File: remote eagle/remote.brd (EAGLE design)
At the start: 38.6 x 38.6 mm, 13 parts, among them J1 ISP Touch, Y1 8MHz

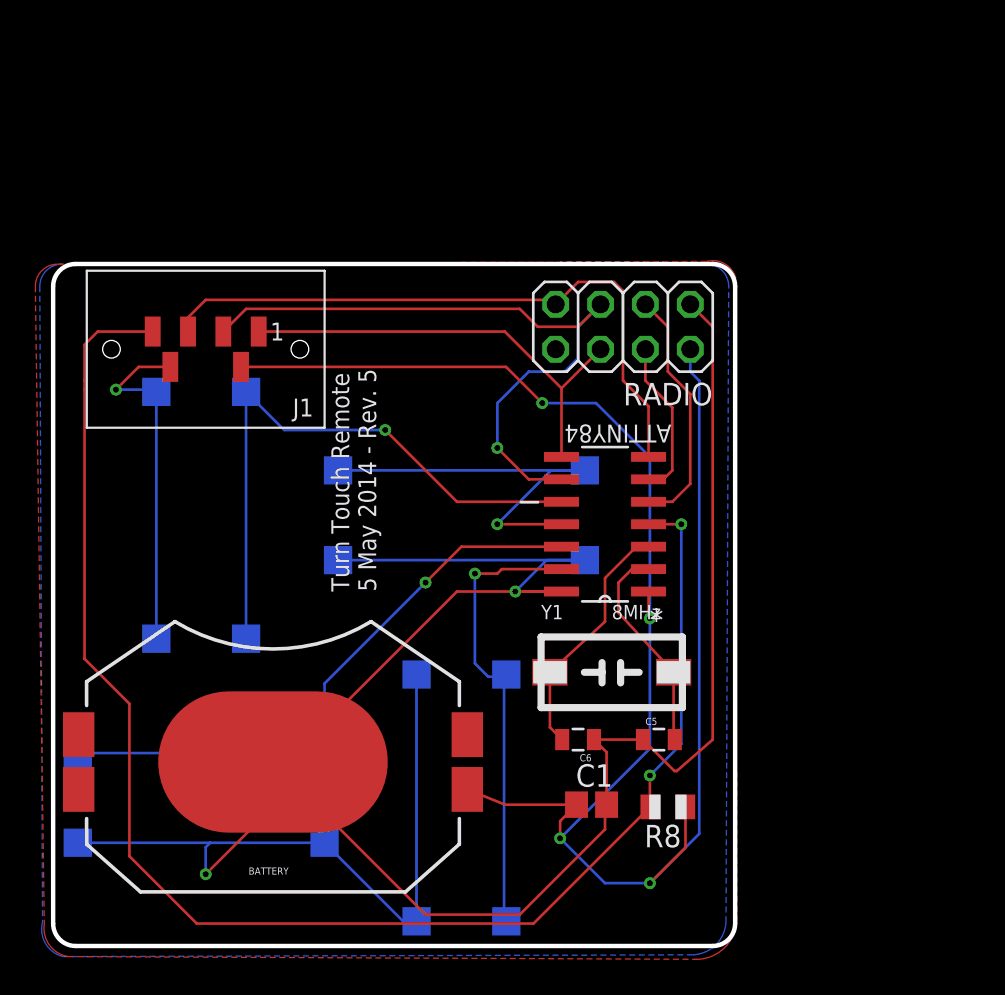
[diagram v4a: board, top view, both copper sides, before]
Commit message: Moving from nrf24L01+ module to onboard chip. Moving both MCU and radio IC to QFN package.
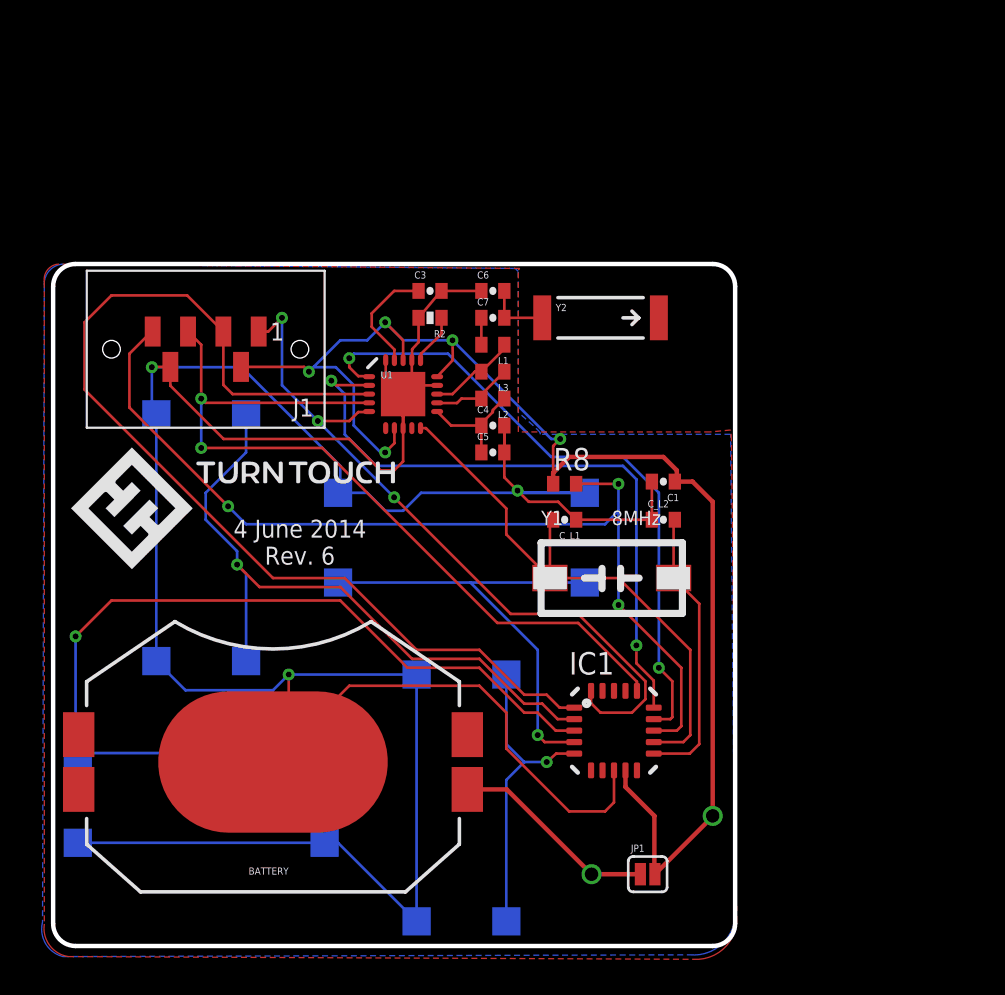
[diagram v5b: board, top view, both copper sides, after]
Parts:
- removed ATTINY84: (no value), Atmel_By_element14_Batch_1:SOIC127P600X175-14N
- removed RADIO: NRF24L01, pinhead:2X04
- added C3: 33nF, SparkFun:0402-CAP
- added C4: 2.2nF, SparkFun:0402-CAP
- added C7: 1.5pF, SparkFun:0402-CAP
- added C_L1, C_L2: 8pF, SparkFun-Passives:0402-CAP
- added IC1: TINY24/44/84-MU, avr-7:QFN/MLF20
- added JP1: (no value), SparkFun-Passives:SJ_2S
- added L1: 3.9nH, SparkFun:C0402
- added L2: 2.7nH, SparkFun:C0402
- added L3: 8.2nH, SparkFun:C0402
- added LOGO: (no value), remote:LOGO
- added R2: 22K, SparkFun:0402-RES
- added U1: NRF24L01ALT1, Testing:QFN20_ALT1
- added Y2: ANTENNA2SMD5, SparkFun:ANTENNA-CHIP5
- C1: value .1uf -> .1uF; device adafruit:C0805 -> SparkFun-Passives:0402-CAP
- C5: value 15pF -> 4.7pF; device SparkFun-Passives:0805 -> SparkFun:0402-CAP
- C6: value 15pF -> 1.0pF; device SparkFun-Passives:0805 -> SparkFun:0402-CAP
- R8: device adafruit:R0805 -> resistor:R0402
- moved C6 25.9 mm to (24.9, 37.1), turned to 0 degrees
- moved R8 19.2 mm to (29.0, 26.2), turned to 0 degrees
- moved C5 18.8 mm to (24.9, 27.9)
- moved C1 18.7 mm to (34.5, 26.3), turned to 180 degrees
- moved Y1 5.33 mm to (31.6, 20.8)
- moved U$2 1.27 mm to (23.1, 23.1), turned to 0 degrees
- moved U$4 1.27 mm to (8.38, 23.1)
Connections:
- new net ANT: C6.2, C7.2, Y2.FEED
- new net N$4: R2.1, U1.16
- new net N$5: C3.1, U1.19
- new net N$6: L1.1, L3.2, U1.13
- new net N$7: C4.1, C5.1, L2.1, U1.11
- new net N$8: L2.2, L3.1, U1.12
- new net N$9: C7.1, L1.2
- new net VMM: BATTERY.1, JP1.1
- net BUTTON1: now also IC1.5; no longer ATTINY84.13
- net BUTTON2: now also IC1.4; no longer ATTINY84.11
- net BUTTON3: now also IC1.3; no longer ATTINY84.12
- net BUTTON4: now also IC1.2; no longer ATTINY84.10
- net CE: now also IC1.14, U1.1; no longer ATTINY84.5, RADIO.3
- net CSN: now also IC1.15, U1.2; no longer ATTINY84.6, RADIO.4
- net GND: now also C3.2, C4.2, C5.2, C_L1.1, C_L2.1, IC1.8, R2.2, U1.0, U1.14, U1.17, U1.20, U1.8; no longer ATTINY84.14, C5.1, RADIO.1
- net MISO: now also IC1.20, U1.5; no longer ATTINY84.8, RADIO.6
- net MOSI: now also IC1.16, U1.4; no longer ATTINY84.7, RADIO.7
- net RESET: now also IC1.13; no longer ATTINY84.4
- net SCK: now also IC1.1, U1.3; no longer ATTINY84.9, RADIO.5
- net VCC: now also IC1.9, JP1.2, U1.15, U1.18, U1.7; no longer ATTINY84.1, BATTERY.1, RADIO.2
- net XTL1: now also C_L2.2, IC1.11; no longer ATTINY84.2, C5.2
- net XTL2: now also C_L1.2, IC1.12, U1.10; no longer ATTINY84.3, C6.2
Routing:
- net RESET: track 86.6 -> 54.9 mm, vias 2 -> 3
- net CSN: track 9.05 -> 36.5 mm, vias 0 -> 2
- net VCC: track 102.0 -> 78.8 mm, vias 4 -> 6
- net CE: track 14.0 -> 36.9 mm, vias 0 -> 2
- net SCK: track 38.9 -> 59.8 mm, vias 1 -> 0
- net BUTTON3: track 34.5 -> 52.7 mm
- net XTL2: track 14.0 -> 31.8 mm
- net GND: track 169.2 -> 186.8 mm
- net MISO: track 25.5 -> 41.4 mm, vias 0 -> 3
- net VMM: track 0.00 -> 11.8 mm, vias 0 -> 1
- net MOSI: track 36.7 -> 47.2 mm, vias 0 -> 2
- net BUTTON1: track 26.1 -> 17.8 mm
- net N$7: track 0.00 -> 6.42 mm
- net N$5: track 0.00 -> 6.36 mm
- net N$6: track 0.00 -> 5.09 mm
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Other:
- board text added: "4 June 2014 Rev. 6"
- board text removed: "Turn Touch Remote 5 May 2014 - Rev. 5"

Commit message: Moving from MFL package to QFN package for ATTiny84A MCU.
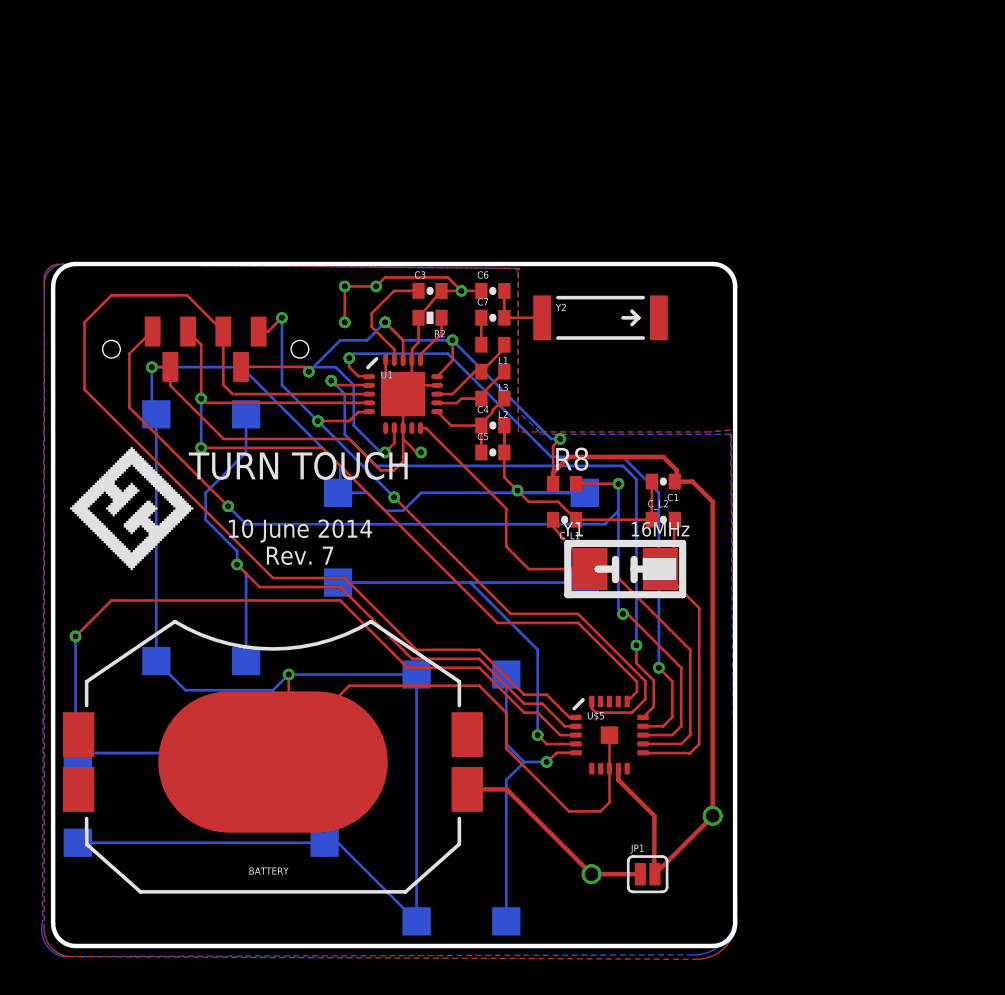
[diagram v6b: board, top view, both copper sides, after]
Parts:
- removed IC1: TINY24/44/84-MU, avr-7:QFN/MLF20
- added U$5: ATTINY24QFN, SparkFun-DigitalIC:QFN20
- Y1: value 8MHz -> 16MHz; device remote:NX8045GB -> remote:NX5032GA
- moved Y1 0.92 mm to (32.4, 21.3)
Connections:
- net BUTTON1: now also U$5.5; no longer IC1.5
- net BUTTON2: now also U$5.4; no longer IC1.4
- net BUTTON3: now also U$5.3; no longer IC1.3
- net BUTTON4: now also U$5.2; no longer IC1.2
- net CE: now also U$5.14; no longer IC1.14
- net CSN: now also U$5.15; no longer IC1.15
- net GND: now also U$5.0, U$5.8; no longer IC1.8
- net MISO: now also U$5.20; no longer IC1.20
- net MOSI: now also U$5.16; no longer IC1.16
- net RESET: now also U$5.13; no longer IC1.13
- net SCK: now also U$5.1; no longer IC1.1
- net VCC: now also U$5.9; no longer IC1.9
- net XTL1: now also U$5.11; no longer IC1.11
- net XTL2: now also U$5.12; no longer IC1.12
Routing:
- net GND: track 186.8 -> 195.5 mm, vias 3 -> 8
- net XTL2: track 31.8 -> 33.2 mm
- net XTL1: track 16.1 -> 17.3 mm
- net RESET: track 54.9 -> 55.7 mm
- net MOSI: track 47.2 -> 48.0 mm
- net CSN: track 36.5 -> 37.3 mm
- net CE: track 36.9 -> 37.6 mm
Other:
- board text added: "10 June 2014 Rev. 7"
- board text added: "TURN TOUCH"
- board text removed: "4 June 2014 Rev. 6"

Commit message: Moving code into src/ and libs/.
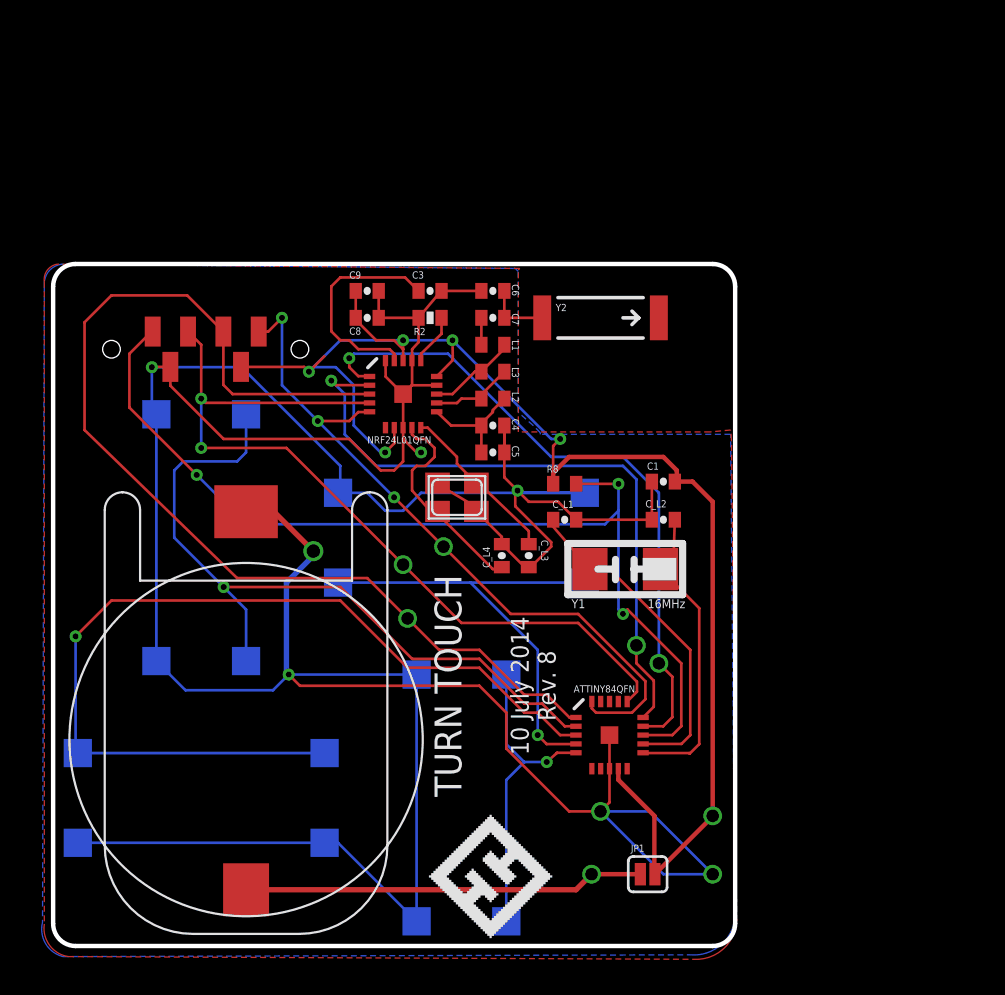
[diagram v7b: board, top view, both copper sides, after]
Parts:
- removed BATTERY: CR2032, SparkFun-Electromechanical:BATTCON_20MM_4LEGS_OVERPASTE
- removed U1: NRF24L01ALT1, Testing:QFN20_ALT1
- added C8: 1nF, SparkFun:0402-CAP
- added C9: 10nF, SparkFun:0402-CAP
- added C_L3, C_L4: 8pF, SparkFun-Passives:0402-CAP
- added NRF24L01QFN: NRF24L01SMD, Testing:QFN20
- added Q1: (no value), adafruit:NX3225
- added U$6: COINCELLHOLDER, remote:20MMCOINCELL
- moved LOGO 34.2 mm to (28.2, 0.51), turned to 90 degrees
- renumbered U$5 to ATTINY84QFN
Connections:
- new net N$2: C_L4.2, NRF24L01QFN.9, Q1.1
- new net N$3: C_L3.2, NRF24L01QFN.10, Q1.3
- net CE: now also NRF24L01QFN.1; no longer U1.1
- net CSN: now also NRF24L01QFN.2; no longer U1.2
- net GND: now also C8.2, C9.2, C_L3.1, C_L4.1, NRF24L01QFN.0, NRF24L01QFN.14, NRF24L01QFN.17, NRF24L01QFN.20, NRF24L01QFN.8, Q1.2, Q1.4, U$6.P$2; no longer BATTERY.2, U1.0, U1.14, U1.17, U1.20, U1.8
- net MISO: now also NRF24L01QFN.5; no longer U1.5
- net MOSI: now also NRF24L01QFN.4; no longer U1.4
- net N$4: now also NRF24L01QFN.16; no longer U1.16
- net N$5: now also NRF24L01QFN.19; no longer U1.19
- net N$6: now also NRF24L01QFN.13; no longer U1.13
- net N$7: now also NRF24L01QFN.11; no longer U1.11
- net N$8: now also NRF24L01QFN.12; no longer U1.12
- net SCK: now also NRF24L01QFN.3; no longer U1.3
- net VCC: now also C8.1, C9.1, NRF24L01QFN.15, NRF24L01QFN.18, NRF24L01QFN.7; no longer U1.15, U1.18, U1.7
- net VMM: now also U$6.P$1; no longer BATTERY.1
- net XTL2: no longer U1.10
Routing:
- net GND: track 195.5 -> 225.2 mm, vias 8 -> 7
- net XTL2: track 33.2 -> 19.0 mm
- net N$2: track 0.00 -> 12.3 mm
- net VMM: track 11.8 -> 22.7 mm
- net N$3: track 0.00 -> 9.96 mm
- net N$5: track 6.36 -> 12.5 mm
- net VCC: track 79.0 -> 83.0 mm
- net BUTTON4: track 38.8 -> 42.3 mm
- net SCK: track 60.1 -> 61.4 mm, vias 0 -> 1
- net MOSI: vias 2 -> 3
- net MISO: track 40.9 -> 41.0 mm, vias 3 -> 4
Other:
- board text added: "10 July 2014 Rev. 8"
- board text removed: "10 June 2014 Rev. 7"

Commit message: Revision 9 of the board. Could perhaps use some tweaking. Now uses atmega328p qfn chip.
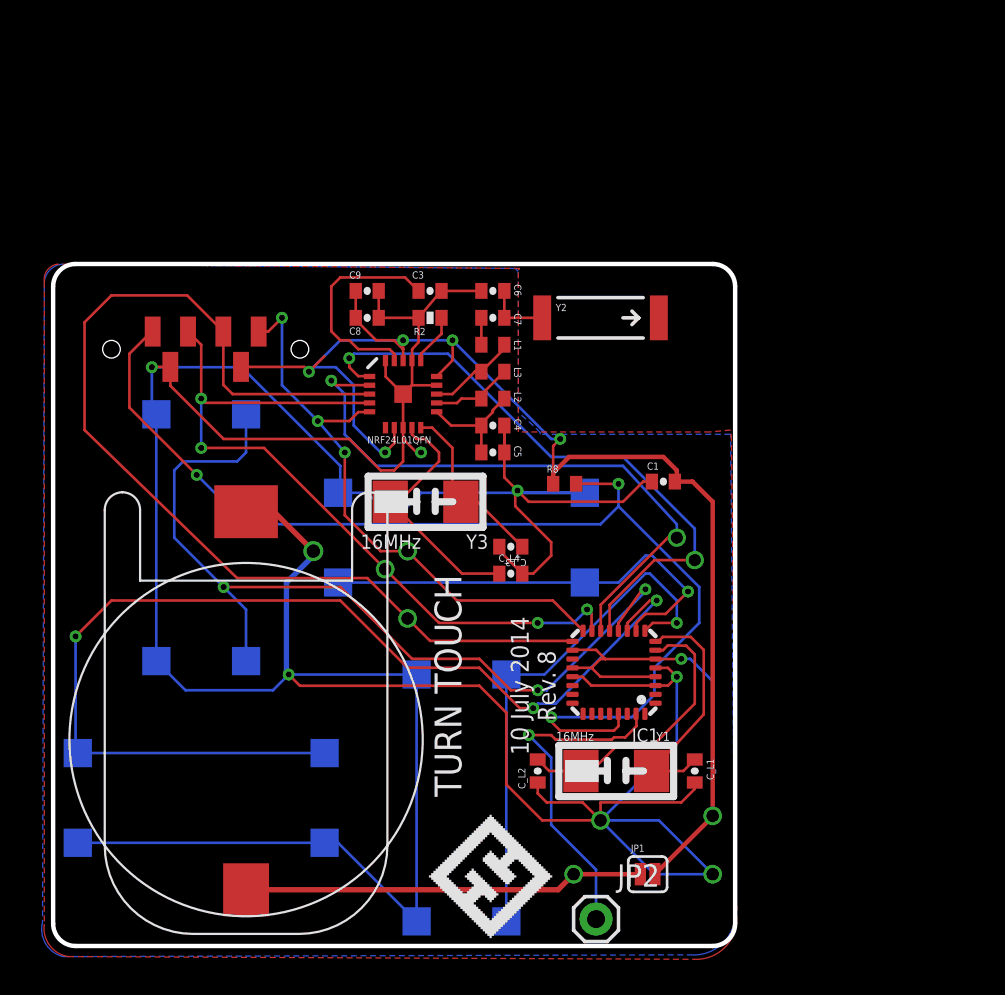
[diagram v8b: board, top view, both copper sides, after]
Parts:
- removed ATTINY84QFN: ATTINY24QFN, SparkFun-DigitalIC:QFN20
- removed Q1: (no value), adafruit:NX3225
- added IC1: ATmega328p, atmel:MLF32
- added JP2: Serial, SparkFun-Connectors:1X01
- added Y3: 16MHz, remote:NX5032GA
- moved C_L1 16.0 mm to (36.3, 9.91), turned to 90 degrees
- moved C_L2 15.9 mm to (27.4, 9.91), turned to 90 degrees
- moved Y1 11.4 mm to (31.9, 9.91), turned to 180 degrees
- moved C_L3 1.14 mm to (25.9, 22.6), turned to 0 degrees
- moved C_L4 1.14 mm to (25.9, 21.1), turned to 180 degrees
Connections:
- new net SERIAL: IC1.31, JP2.1
- net BUTTON1: now also IC1.9; no longer ATTINY84QFN.5
- net BUTTON2: now also IC1.10; no longer ATTINY84QFN.4
- net BUTTON3: now also IC1.11; no longer ATTINY84QFN.3
- net BUTTON4: now also IC1.12; no longer ATTINY84QFN.2
- net CE: now also IC1.13; no longer ATTINY84QFN.14
- net CSN: now also IC1.14; no longer ATTINY84QFN.15
- net GND: now also IC1.21, IC1.3, IC1.5; no longer ATTINY84QFN.0, ATTINY84QFN.8, Q1.2, Q1.4
- net MISO: now also IC1.16; no longer ATTINY84QFN.20
- net MOSI: now also IC1.15; no longer ATTINY84QFN.16
- net N$2: now also Y3.P$2; no longer Q1.1
- net N$3: now also Y3.P$1; no longer Q1.3
- net RESET: now also IC1.29; no longer ATTINY84QFN.13
- net SCK: now also IC1.17; no longer ATTINY84QFN.1
- net VCC: now also IC1.18, IC1.20, IC1.4, IC1.6; no longer ATTINY84QFN.9
- net XTL1: now also IC1.7; no longer ATTINY84QFN.11
- net XTL2: now also IC1.8; no longer ATTINY84QFN.12
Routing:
- net SERIAL: track 0.00 -> 19.2 mm, vias 0 -> 1
- net GND: track 225.2 -> 243.7 mm, vias 7 -> 8
- net VCC: track 83.0 -> 98.5 mm, vias 6 -> 7
- net BUTTON1: track 17.9 -> 29.9 mm
- net BUTTON3: track 53.0 -> 62.1 mm, vias 1 -> 3
- net BUTTON4: track 42.3 -> 50.8 mm, vias 1 -> 3
- net RESET: track 56.1 -> 64.5 mm
- net MISO: track 41.0 -> 33.6 mm
- net XTL2: track 19.0 -> 13.9 mm
- net MOSI: track 48.0 -> 44.1 mm, vias 3 -> 5
- net CE: track 37.6 -> 34.7 mm
- net CSN: track 37.3 -> 34.7 mm
- net N$2: track 12.3 -> 14.4 mm
- net SCK: track 61.4 -> 59.4 mm
- net BUTTON2: track 26.6 -> 25.4 mm
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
